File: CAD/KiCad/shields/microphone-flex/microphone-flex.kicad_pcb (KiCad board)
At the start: 2 copper layers, 32 x 62 mm, 22 parts, among them J1 GND / +5V / OUT, J2 LEFT / 1x05 RIGHT ANGLE, J3 RIGHT / 1x05 RIGHT ANGLE, M1 UP / ONE MODULE ONLY

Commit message: Restore removable microphone gain and A/R selectors across flex design
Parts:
- removed R1: 0R / GAIN VDD 40dB, Shields:R_0603_1608Metric
- removed R2: 0R / AR GND 1:500, Shields:R_0603_1608Metric
- added JP1: GAIN SELECT / HEADER + SHUNT, Shields:Flex_Gain_Selector, F.Cu at (51.2, 88.0)
- added JP2: AR SELECT / HEADER + SHUNT, Shields:Flex_AR_Selector, F.Cu at (68.8, 88.0)
- moved C6 1.50 mm to (68.0, 96.5)
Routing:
- net MICOUT: track 48.0 -> 41.9 mm, vias 0 -> 1
- net GAIN: track 25.3 -> 31.2 mm
- net GND: track 77.0 -> 82.7 mm, vias 0 -> 1
- net led/D1: track 41.7 -> 36.5 mm, vias 2 -> 0
- net VDD: track 82.6 -> 80.3 mm, vias 3 -> 1
- net AR: track 37.2 -> 38.1 mm
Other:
- board text added: "50/60/40"
- board text added: "500/4K/2K"
- board text added: "COLLOQUY MIC C-J"
- board text added: "JP1 GAIN"
- board text added: "JP2 A/R"
- board text removed: "COLLOQUY MIC C"

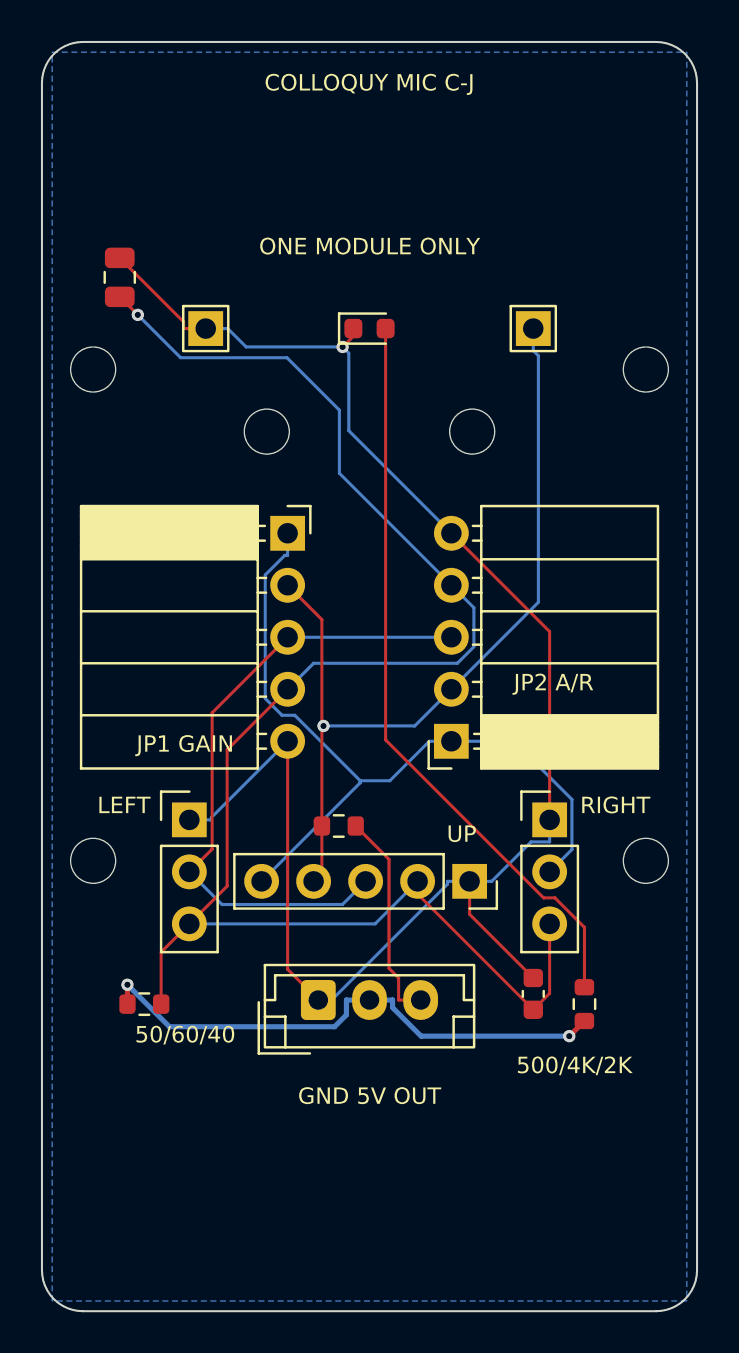
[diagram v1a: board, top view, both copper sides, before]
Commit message: Reroute microphone flex around the approved component placement
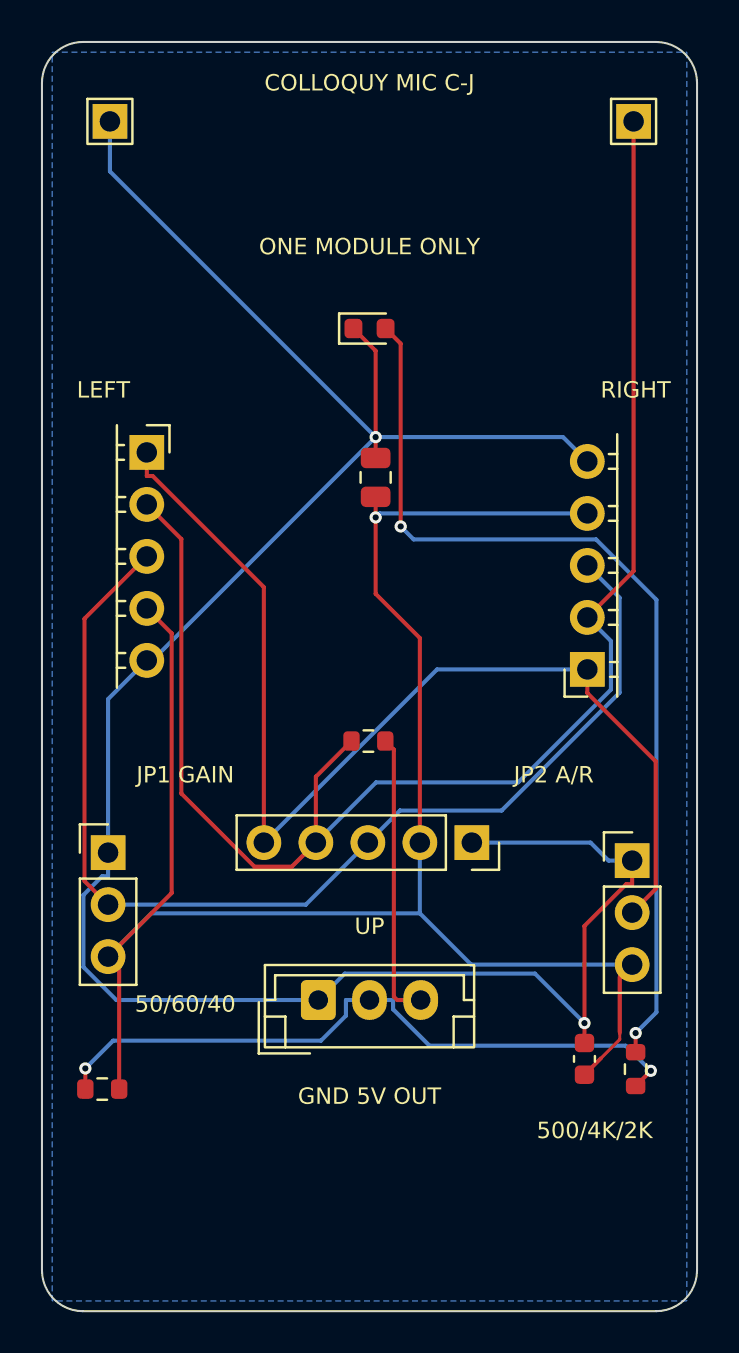
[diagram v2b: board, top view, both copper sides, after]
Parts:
- removed H3, H4: M2 MODULE / INSULATING SPACER, Shields:Flex_M2_Top
- removed H5, H6, H7, H8: M2 SIDE SUPPORT BASE, Shields:Flex_M2_Base
- J2: footprint Shields:Flex_Socket_Side -> Shields:Flex_Socket_Left_Overhang
- J3: footprint Shields:Flex_Socket_Side -> Shields:Flex_Socket_Right_Overhang
- moved C7 15.9 mm to (60.3, 71.3)
- moved TP1 11.2 mm to (72.9, 53.9)
- moved TP2 11.1 mm to (47.3, 53.9)
- moved J2 7.93 mm to (49.1, 70.0)
- moved J3 7.51 mm to (70.6, 80.7)
- moved R4 4.63 mm to (46.9, 101.2)
- moved JP2 4.49 mm to (72.8, 90.0)
- moved R5 4.39 mm to (59.9, 84.2)
- moved JP1 4.28 mm to (47.2, 89.6)
- moved C6 4.04 mm to (70.5, 99.7)
- moved R6 4.04 mm to (73.0, 100.2)
- moved M1 1.90 mm to (65.0, 89.1)
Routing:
- net MICOUT: track 41.9 -> 75.7 mm, vias 1 -> 0
- net GND: track 82.7 -> 115.4 mm, vias 1 -> 2
- net GAIN: track 31.2 -> 54.9 mm
- net AR: track 38.1 -> 54.6 mm
- net VDD: track 80.3 -> 91.0 mm
- net led/D1: track 36.5 -> 46.5 mm, vias 0 -> 2
- net +5V: track 26.3 -> 33.2 mm
- net OUT: track 10.4 -> 14.0 mm

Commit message: Flip side microphones below the carrier and reverse their pin mapping
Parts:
- J2: value LEFT / 1x05 RIGHT ANGLE -> LEFT / DOWNWARD MODULE
- J3: value RIGHT / 1x05 RIGHT ANGLE -> RIGHT / DOWNWARD MODULE
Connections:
- J2 pad 1: AR -> GND
- J2 pad 2: MICOUT -> VDD
- J2 pad 4: VDD -> MICOUT
- J2 pad 5: GND -> AR
- J3 pad 1: AR -> GND
- J3 pad 2: MICOUT -> VDD
- J3 pad 4: VDD -> MICOUT
- J3 pad 5: GND -> AR
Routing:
- net MICOUT: track 75.7 -> 65.1 mm
- net AR: track 54.6 -> 64.2 mm
- net GAIN: track 54.9 -> 50.1 mm
- net VDD: track 91.0 -> 87.6 mm
- net led/D1: track 46.5 -> 44.2 mm
- net GND: track 115.4 -> 117.1 mm
